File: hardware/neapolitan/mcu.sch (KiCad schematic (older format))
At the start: 43 parts, among them J1 USB-MICRO-B, J11 BARREL_JACK, P1 !IO_INT, P2 !IO_RESET, P20 GPIO, P22 I2S, P28 SD, P5 LEDS, P80 SHIELD, Q5 MOSFET_P, U15 TCA6424A, X2 FOX924B

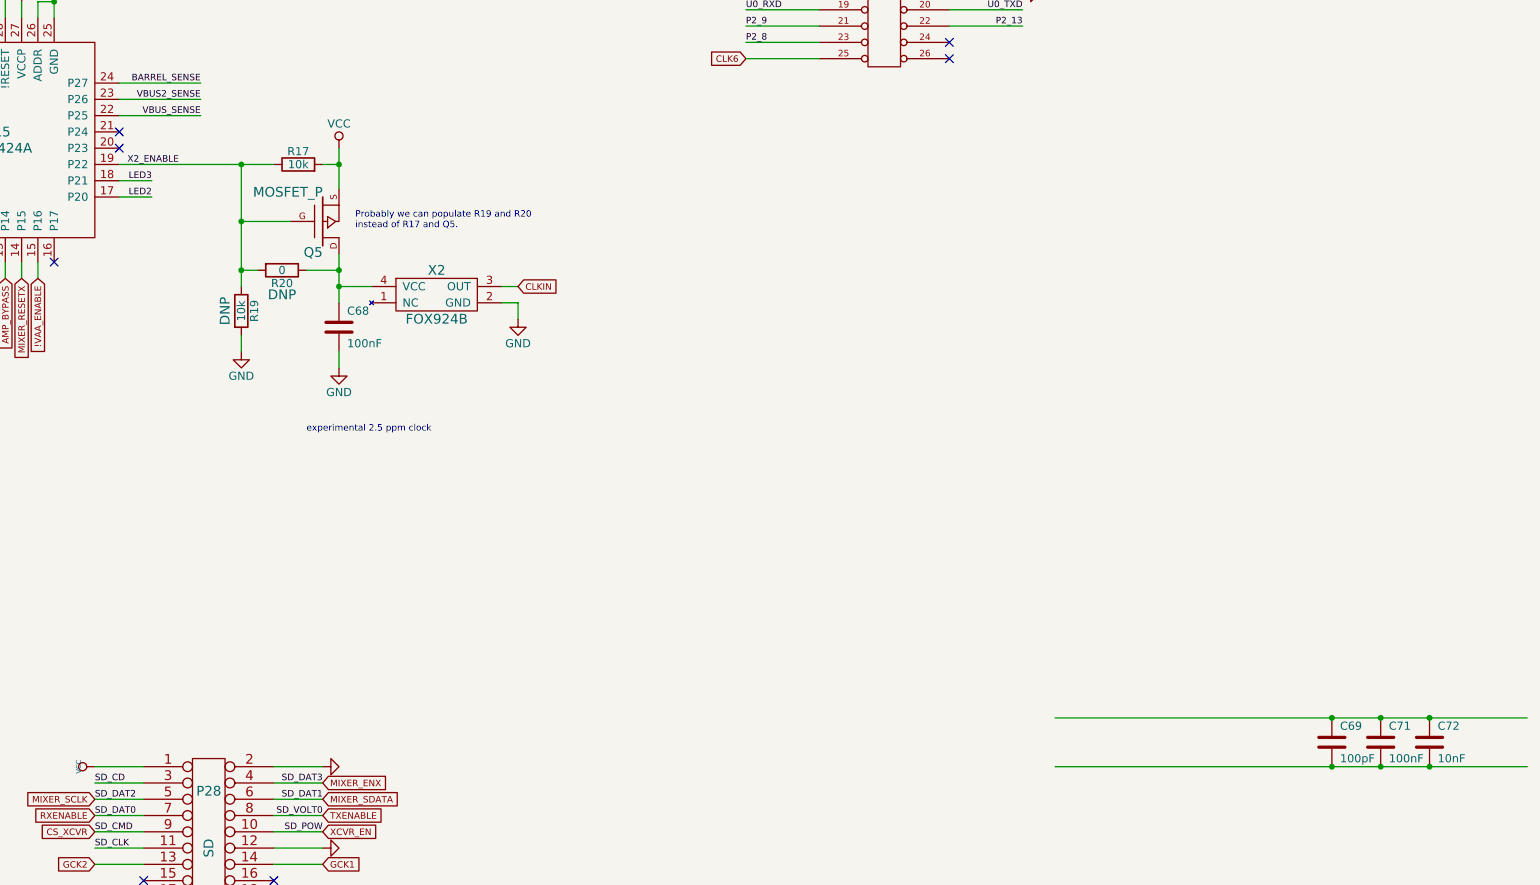
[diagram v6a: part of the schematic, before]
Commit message: Neapolitan: experimental 500 ppb clock in schematic
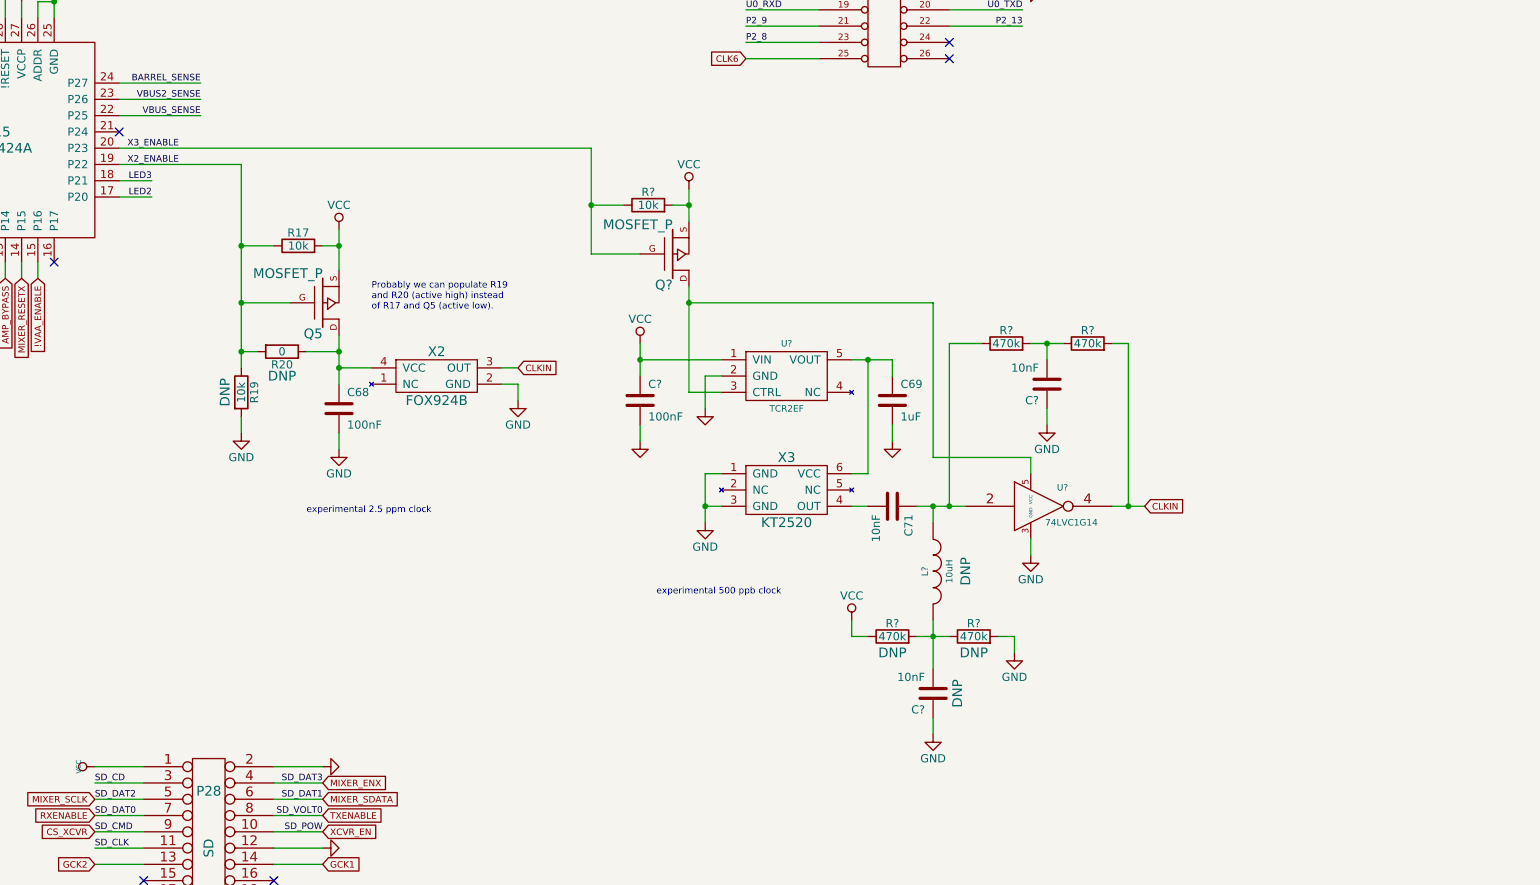
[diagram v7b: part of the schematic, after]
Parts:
- removed C72: 10nF, hackrf:GSG-0402, symbol C
- added C?: 100nF, hackrf:GSG-0402, symbol C
- added C? (x2): 10nF, hackrf:GSG-0402, symbol C
- added L?: 10uH, hackrf:GSG-0603, symbol INDUCTOR
- added Q?: MOSFET_P, gsg-modules:SOT23GDS, symbol MOSFET_P
- added R? (x4): 470k, hackrf:GSG-0603, symbol R
- added R?: 10k, hackrf:GSG-0402, symbol R
- added U?: TCR2EF, symbol TCR2EF
- added U?: 74LVC1G14, symbol 74AHC1G14
- added X3: KT2520, symbol KT2520
- C69: value 100pF -> 1uF; Description CAP CER 100PF 50V 5% NP0 0402 -> CAP CER 1UF 10V 10% X5R 0402; Manufacturer Murata -> Taiyo Yuden; Part Number GRM1555C1H101JA01D -> LMK105BJ105KV-F
- C71: value 100nF -> 10nF; Description CAP CER 0.1UF 10V 10% X5R 0402 -> CAP CER 10000PF 16V 10% X7R 0402; Part Number GRM155R61A104KA01D -> GRM155R71C103KA01D
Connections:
- net CLKIN: now also R?.2, U?.4
- net GND: now also C69.2, C?.1, C?.1, C?.2, R?.2, U?.2 (GND), U?.3 (GND), X3.1 (GND), X3.3 (GND)
- net VCC: now also C?.1, Q?.S, R?.1, R?.2, U?.1 (VIN)
- net X3_ENABLE: now reaches U15.20 (P23)
- net X3_ENABLE: now also Q?.G, R?.1
- net at C69.1: now also U?.5 (VOUT), X3.6 (VCC); no longer C71.1
- net at C71.2: now also X3.4 (OUT); no longer C69.2
- new net: C71.1, L?.1, R?.1, U?.2
- new net: Q?.D, U?.3 (CTRL), U?.5 (VCC)
- new net: C?.2, R?.1, R?.2
- new net: C?.2, L?.2, R?.1, R?.2
- no-connect marks 18 -> 17
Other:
- note added: "Probably we can populate R19\nand R20 (active high) instead\nof R17 and Q5 (active low)."
- note added: "experimental 500 ppb clock"
- note removed: "Probably we can populate R19 and R20\ninstead of R17 and Q5."
- moved on the sheet: C68, Q5, R17, R19, R20, X2

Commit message: Neapolitan: experimental 10 ppb clock in schematic
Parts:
- added C?: 10nF, hackrf:GSG-0402, symbol C
- added C?: 22pF, hackrf:GSG-0402, symbol C
- added Q?: MOSFET_P, gsg-modules:SOT23GDS, symbol MOSFET_P
- added R?: 10k, hackrf:GSG-0402, symbol R
- added X4: OH4, symbol OH4
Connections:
- net CLKIN: now also C?.1, X4.8 (OUT)
- net GND: now also C?.1, C?.2, X4.7 (GND)
- net VCC: now also Q?.S, R?.2
- net X4_ENABLE: now reaches U15.21 (P24)
- net X4_ENABLE: now also Q?.G, R?.1
- new net: C?.2, Q?.D, X4.14 (VCC)
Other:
- note added: "experimental 10 ppb clock"
